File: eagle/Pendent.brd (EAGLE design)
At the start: 40.6 x 40.6 mm, 25 parts, among them Q1 CMA-4544PF-W, U1 Tiny85-20-SMT, U2 LF50ABDT-TR

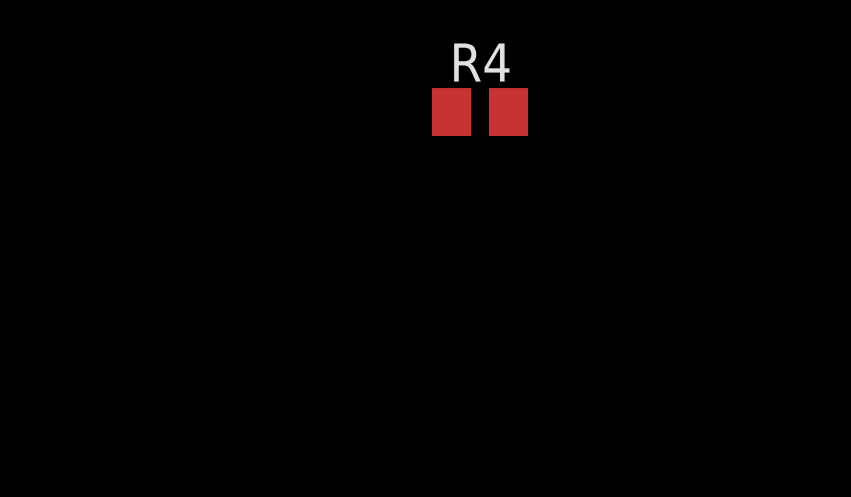
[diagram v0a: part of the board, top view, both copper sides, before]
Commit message: Add IRSend add IR LED to schematic
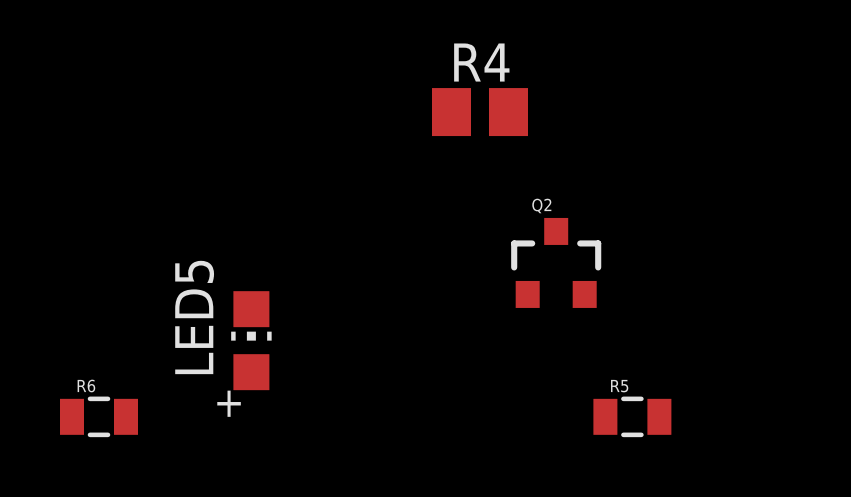
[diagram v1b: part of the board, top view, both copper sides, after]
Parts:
- added LED5: XZTNI54W, adafruit:CHIP-LED0805
- added Q2: MPSA42, SparkFun-DiscreteSemi:SOT23-3
- added R5: 1k, SparkFun-Passives:0805
- added R6: 20, SparkFun-Passives:0805
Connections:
- new net N$13: Q2.1, R5.2
- new net N$15: LED5.C, Q2.3
- new net N$16: LED5.A, R6.2
- new net N$17: R5.1, U1.6
- net GND: now also Q2.2
- net N$12: now also U1.7; no longer U1.6
- net N$4: now also U1.3; no longer U1.5
- net VCC: now also R6.1
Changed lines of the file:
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@@
 </element>
 <element name="R4" library="adafruit" package="M0805" value="" x="2.54" y="-40.64"/>
+<element name="Q2" library="SparkFun-DiscreteSemi" package="SOT23-3" value="MPSA42" x="5.08" y="-45.72">
+<attribute name="VALUE" value="MPSA42" x="5.08" y="-45.72" size="1.778" layer="27" display="off"/>
+<attribute name="PROD_ID" value="TRANS-09116" x="5.08" y="-45.72" size="1.778" layer="27" display="off"/>
+</element>
+<element name="R5" library="SparkFun-Passives" package="0805" value="1k" x="7.62" y="-50.8"/>
+<element name="LED5" library="adafruit" package="CHIP-LED0805" value="XZTNI54W" x="-5.08" y="-48.26"/>
+<element name="R6" library="SparkFun-Passives" package="0805" value="20" x="-10.16" y="-50.8"/>
 </elements>
 <signals>
@@
 <contactref element="S1" pad="3"/>
 <contactref element="S1" pad="4"/>
-<wire x1="31.545" y1="25" x2="31.545" y2="26.2" width="0" layer="19" extent="1-1"/>
-<wire x1="22.186" y1="22.86" x2="31.545" y2="25" width="0" layer="19" extent="1-1"/>
-<wire x1="20.283" y1="20.65" x2="22.186" y2="22.86" width="0" layer="19" extent="1-1"/>
-<wire x1="17.52" y1="16.28" x2="20.283" y2="20.65" width="0" layer="19" extent="1-1"/>
-<wire x1="15.864" y1="13.208" x2="17.52" y2="16.28" width="0" layer="19" extent="1-1"/>
-<wire x1="13.335" y1="10.4648" x2="15.864" y2="13.208" width="0" layer="19" extent="1-1"/>
+<contactref element="R6" pad="1"/>
+<wire x1="2.286" y1="-34.925" x2="-11.06" y2="-50.8" width="0" layer="19" extent="1-1"/>
+<wire x1="7.874" y1="-34.925" x2="2.286" y2="-34.925" width="0" layer="19" extent="1-1"/>
+<wire x1="9.16" y1="-27.94" x2="7.874" y2="-34.925" width="0" layer="19" extent="1-1"/>
+<wire x1="2.54" y1="7.962" x2="9.16" y2="-27.94" width="0" layer="19" extent="1-1"/>
+<wire x1="13.335" y1="10.4648" x2="2.54" y2="7.962" width="0" layer="19" extent="1-1"/>
+<wire x1="15.864" y1="13.208" x2="13.335" y2="10.4648" width="0" layer="19" extent="1-1"/>
+<wire x1="17.52" y1="16.28" x2="15.864" y2="13.208" width="0" layer="19" extent="1-1"/>
+<wire x1="20.283" y1="20.65" x2="17.52" y2="16.28" width="0" layer="19" extent="1-1"/>
+<wire x1="22.186" y1="22.86" x2="20.283" y2="20.65" width="0" layer="19" extent="1-1"/>
 <wire x1="22.186" y1="10.16" x2="15.864" y2="13.208" width="0" layer="19" extent="1-1"/>
-<wire x1="2.54" y1="7.962" x2="13.335" y2="10.4648" width="0" layer="19" extent="1-1"/>
+<wire x1="31.545" y1="25" x2="22.186" y2="22.86" width="0" layer="19" extent="1-1"/>
+<wire x1="31.545" y1="26.2" x2="31.545" y2="25" width="0" layer="19" extent="1-1"/>
 <wire x1="6.438" y1="23.368" x2="17.52" y2="16.28" width="0" layer="19" extent="1-1"/>
-<wire x1="9.16" y1="-27.94" x2="2.54" y2="7.962" width="0" layer="19" extent="1-1"/>
-<wire x1="7.874" y1="-34.925" x2="9.16" y2="-27.94" width="0" layer="19" extent="1-1"/>
-<wire x1="2.286" y1="-34.925" x2="7.874" y2="-34.925" width="0" layer="19" extent="1-1"/>
 </signal>
 <signal name="GND">
@@
 <contactref element="C11" pad="2"/>
 <contactref element="R4" pad="1"/>
+<contactref element="Q2" pad="2"/>
 <wire x1="34.495" y1="25.4" x2="34.32" y2="29.94" width="0" layer="19" extent="1-1"/>
 <wire x1="33.02" y1="25.4" x2="34.495" y2="25.4" width="0" layer="19" extent="1-1"/>
@@
 <wire x1="18.78" y1="-22.86" x2="11.16" y2="-27.94" width="0" layer="19" extent="1-1"/>
 <wire x1="1.59" y1="-40.64" x2="3.54" y2="-27.94" width="0" layer="19" extent="1-1"/>
+<wire x1="6.03" y1="-46.72" x2="1.59" y2="-40.64" width="0" layer="19" extent="1-1"/>
 </signal>
 <signal name="N$1">
@@
 </signal>
 <signal name="N$4">
-<contactref element="U1" pad="5"/>
 <contactref element="LED1" pad="4"/>
-<wire x1="17.145" y1="10.4648" x2="25.437" y2="20.65" width="0" layer="19" extent="1-1"/>
+<contactref element="U1" pad="3"/>
+<wire x1="15.875" y1="3.7338" x2="25.437" y2="20.65" width="0" layer="19" extent="1-1"/>
 </signal>
 <signal name="VDD">
@@
 <contactref element="S1" pad="1"/>
 <contactref element="S1" pad="2"/>
-<contactref element="U1" pad="6"/>
+<contactref element="U1" pad="7"/>
 <wire x1="2.286" y1="-31.115" x2="3.49" y2="-40.64" width="0" layer="19" extent="1-1"/>
 <wire x1="7.874" y1="-31.115" x2="2.286" y2="-31.115" width="0" layer="19" extent="1-1"/>
-<wire x1="15.875" y1="10.4648" x2="7.874" y2="-31.115" width="0" layer="19" extent="1-1"/>
+<wire x1="14.605" y1="10.4648" x2="7.874" y2="-31.115" width="0" layer="19" extent="1-1"/>
+</signal>
+<signal name="N$13">
+<contactref element="Q2" pad="1"/>
+<contactref element="R5" pad="2"/>
+<wire x1="8.52" y1="-50.8" x2="4.13" y2="-46.72" width="0" layer="19" extent="1-1"/>
+</signal>
+<signal name="N$15">
+<contactref element="Q2" pad="3"/>
+<contactref element="LED5" pad="C"/>
+<wire x1="5.08" y1="-44.62" x2="-5.08" y2="-47.21" width="0" layer="19" extent="1-1"/>
+</signal>
+<signal name="N$16">
+<contactref element="R6" pad="2"/>
+<contactref element="LED5" pad="A"/>
+<wire x1="-5.08" y1="-49.31" x2="-9.26" y2="-50.8" width="0" layer="19" extent="1-1"/>
+</signal>
+<signal name="N$17">
+<contactref element="U1" pad="6"/>
+<contactref element="R5" pad="1"/>
+<wire x1="15.875" y1="10.4648" x2="6.72" y2="-50.8" width="0" layer="19" extent="1-1"/>
 </signal>
 </signals>

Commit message: Board Layout
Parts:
- added JP10: (no value), SparkFun-Connectors:1X06
- added R7: 300, adafruit:M0805
- added S2: SWITCH-MOMENTARY-2SMD-REDUNDANT, SparkFun-Electromechanical:TACTILE-SWITCH-SMD
- C2, C3, C4, C5: device SparkFun-Capacitors:0603-CAP -> adafruit:C0805K
- C8, C9: device SparkFun-Capacitors:0805 -> adafruit:C0805K
- R4: value (none) -> 10k
- U$3: value (none) -> 6V; device adafruit:CR2032-SMD -> SparkFun-Electromechanical:BATTCON_20MM
- moved R6 79.3 mm to (36.6, 13.2), flipped to the bottom, turned to 270 degrees
- moved R5 69.1 mm to (33.5, 13.2), flipped to the bottom, turned to 270 degrees
- moved LED5 66.3 mm to (35.6, 4.06), flipped to the bottom, turned to 270 degrees
- moved Q2 62.1 mm to (35.1, 8.64), flipped to the bottom, turned to 180 degrees
- moved C10 51.8 mm to (23.9, 19.3), turned to 90 degrees
- moved R4 50.8 mm to (4.57, 10.2), flipped to the bottom
- moved C1 46.9 mm to (17.8, 23.4), turned to 90 degrees
- moved C6 45.1 mm to (13.7, 20.8), turned to 180 degrees
- moved C11 44.8 mm to (23.9, 14.7), turned to 270 degrees
- moved S1 38.6 mm to (6.60, 5.59), flipped to the bottom
- moved R3 36.0 mm to (13.7, 18.0)
- moved C7 35.7 mm to (20.8, 12.7), turned to 270 degrees
- moved R1 34.9 mm to (13.7, 15.2), turned to 180 degrees
- moved R2 31.3 mm to (17.3, 12.7), turned to 90 degrees
- moved Q1 27.0 mm to (7.87, 18.0), turned to 270 degrees
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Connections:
- removed net GAIN: U$1.P$10
- removed net N$12: R4.2, S1.1, S1.2, U1.7
- removed net N$17: R5.1, U1.6
- removed net VDD: LED2.1, LED3.1, LED4.1
- new net MISO: JP10.3, R5.1, U1.6
- new net MOSI: JP10.4, U1.5
- new net N$18: LED1.4, R7.1
- new net RST: JP10.1, S2.1, S2.2, U1.1
- new net SCK: JP10.2, R4.2, S1.1, S1.2, U1.7
- net GND: now also C2.2, C3.2, C4.2, C5.2, JP10.5, U$3.2; no longer C2.1, C3.1, C4.1, C5.1, U$3.-
- net N$2: now also LED2.2
- net N$3: now also LED3.2
- net N$4: now also R7.2; no longer LED1.4
- net N$6: now also U$3.1; no longer U$3.+$1, U$3.+$2
- net VCC: now also C2.1, C3.1, C4.1, C5.1, JP10.6, LED2.1, LED3.1, LED4.1, S2.3, S2.4, U$1.P$10; no longer C2.2, C3.2, C4.2, C5.2
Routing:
- net VCC: track 0.00 -> 175.7 mm, vias 0 -> 4
- net SCK: track 0.00 -> 60.6 mm, vias 0 -> 2
- net N$3: track 0.00 -> 45.4 mm
- net RST: track 0.00 -> 36.8 mm, vias 0 -> 2
- net N$6: track 0.00 -> 30.4 mm, vias 0 -> 1
- net MOSI: track 0.00 -> 29.0 mm
- net MISO: track 0.00 -> 27.7 mm, vias 0 -> 1
- net INPUT: track 0.00 -> 23.7 mm
- net N$4: track 0.00 -> 21.9 mm
- net N$22: track 0.00 -> 21.7 mm, vias 0 -> 2
- net N$2: track 0.00 -> 16.6 mm
- net N$16: track 0.00 -> 11.0 mm
- net N$14: track 0.00 -> 9.83 mm
- net GND: track 0.00 -> 7.35 mm, vias 0 -> 13
- net N$11: track 0.00 -> 6.81 mm
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- added copper zone on layer 1, net GND
- added copper zone on layer 16, net GND
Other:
- board text added: "GND"
- board text added: "RESET"
- board text added: "RST"
- board text added: "VCC"

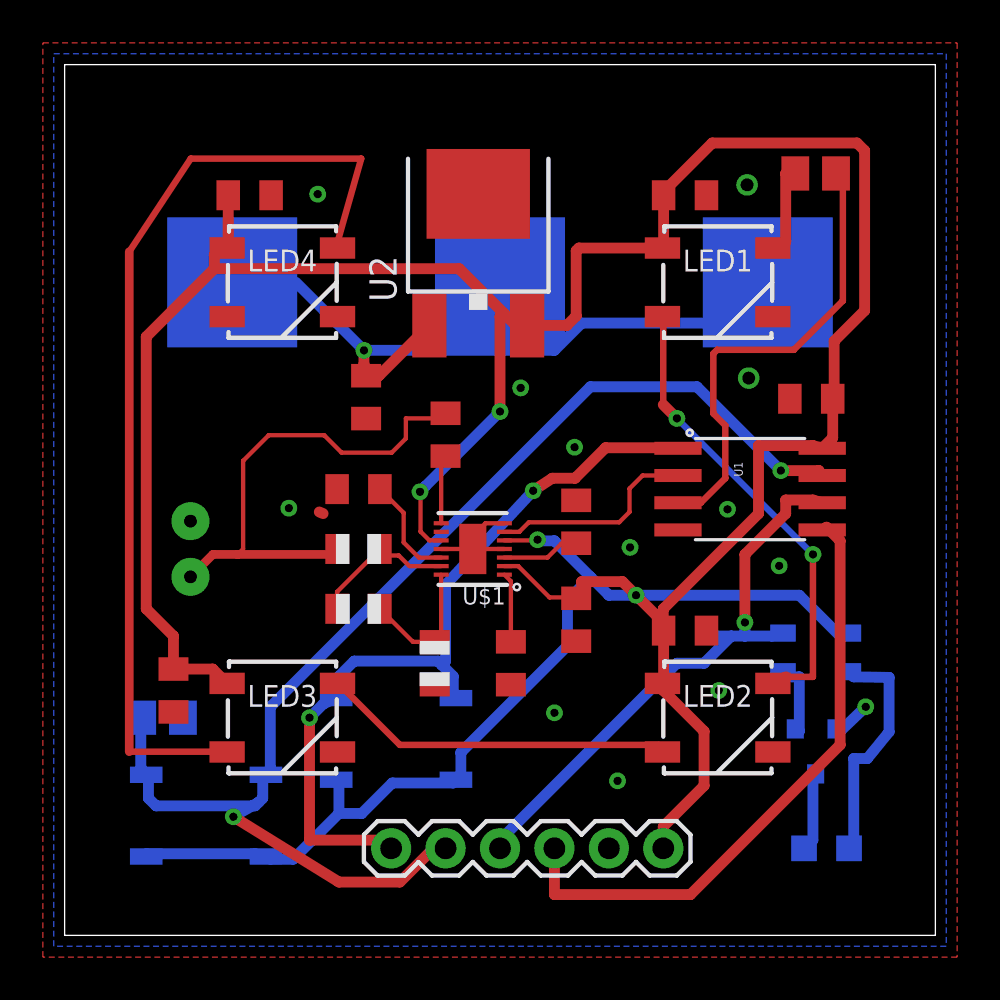
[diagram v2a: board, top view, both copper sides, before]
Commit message: Modificaitons to Board to Accomidate ATmega328P-AU
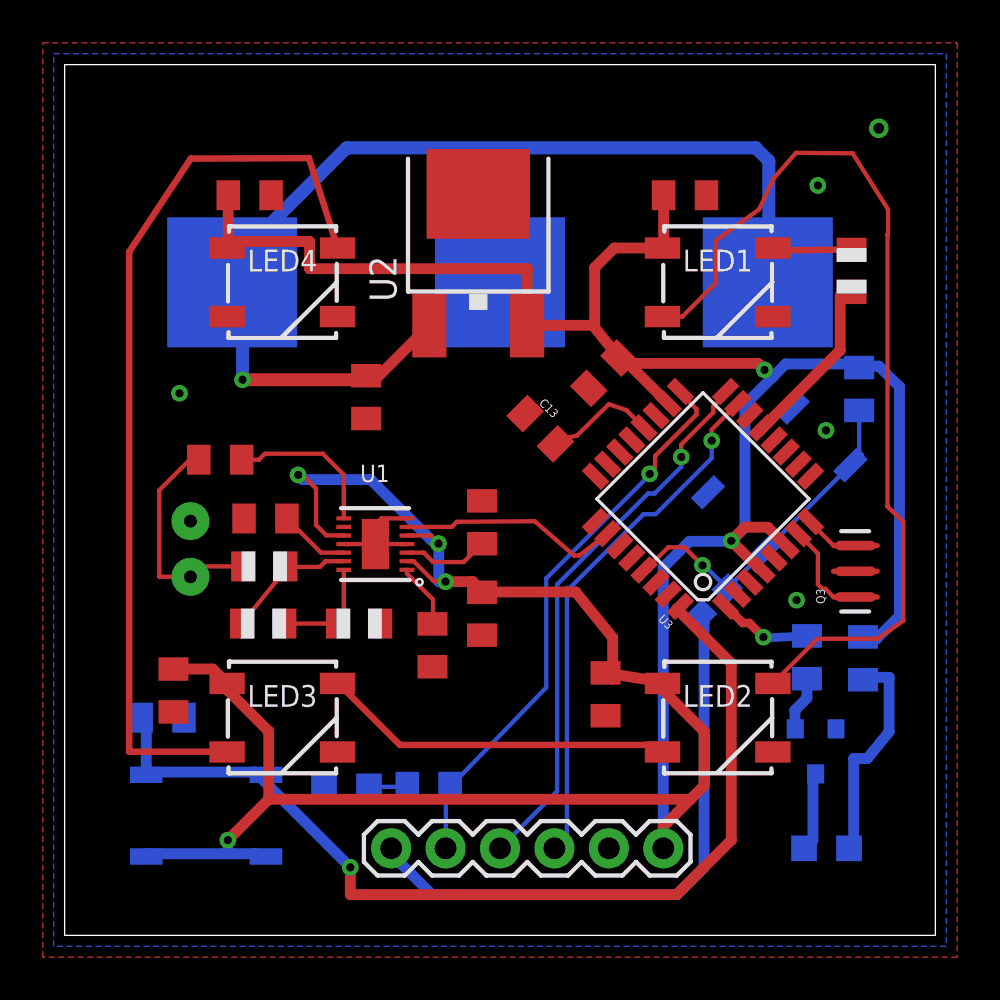
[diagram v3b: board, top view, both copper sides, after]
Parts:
- removed S2: SWITCH-MOMENTARY-2SMD-REDUNDANT, SparkFun-Electromechanical:TACTILE-SWITCH-SMD
- removed U$1: MAX9814TDFN14, adafruit:TDFN14_3X3MM
- added C13: 0.1uF, adafruit:C0805K
- added C14: 0.1uF, SparkFun:0603-CAP
- added D3: Green, adafruit:CHIPLED_0805
- added Q3: 8/16/20MHz, Testing:RESONATOR-SMD-1:1
- added R8: 10K, adafruit:R0805
- added R9: 330, adafruit:R0805
- added S3: RESET, Testing:TACTILE-SWITCH-SMD-ALT01
- added U3: ATMEGA328, SparkFun:TQFP32-08
- C8: value 0.1uF -> 2.2uF
- R4, R7: device adafruit:M0805 -> adafruit:R0805
- R5, R6: device SparkFun-Passives:0805 -> adafruit:R0805
- S1: value SWITCH-MOMENTARY-2SMD-REDUNDANT -> Tempo
- U1: value Tiny85-20-SMT -> MAX9814TDFN14; device SparkFun-DigitalIC:SO08-EIAJ -> adafruit:TDFN14_3X3MM
- moved U1 17.7 mm to (14.5, 18.3), turned to 180 degrees
- moved C1 10.6 mm to (7.26, 22.2), turned to 180 degrees
- moved C9 9.75 mm to (25.2, 26.2), turned to 225 degrees
- moved R7 4.85 mm to (36.7, 31.0), turned to 270 degrees
- moved C3 4.75 mm to (25.2, 11.3), turned to 270 degrees
- moved C6 4.55 mm to (9.37, 19.5)
- moved R1 4.50 mm to (9.27, 14.6)
- moved R3 4.47 mm to (9.32, 17.2)
- moved C11 4.40 mm to (19.5, 15.0)
- moved C10 4.39 mm to (19.5, 19.3)
- moved R2 3.99 mm to (13.7, 14.6), turned to 180 degrees
- moved C7 3.75 mm to (17.2, 13.5)
- moved R5 1.14 mm to (34.6, 13.0)
- moved R6 0.74 mm to (37.3, 12.9)
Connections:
- net N$6 renamed VBATT
- removed net N$14: U$1.P$6, U1.2
- removed net N$4: R7.2, U1.3
- new net A0: U3.23
- new net A1: U3.24
- new net A2: U3.25
- new net A3: U1.P$6, U3.26
- new net A6: U3.19
- new net A7: U3.22
- new net AREF: C13.2, U3.20
- new net D10: U3.14
- new net D2: R4.2, S1.1, S1.2, U3.32
- new net D3: R5.1, U3.1
- new net D4: U3.2
- new net D5: U3.9
- new net D6: U3.10
- new net D7: U3.11
- new net D8: U3.12
- new net D9: R7.2, U3.13
- new net N$1: D3.A, R9.2
- new net N$12: Q3.3, U3.8
- new net N$17: Q3.1, U3.7
- new net RESET: C14.1, R8.1, S3.3, S3.4, U3.29
- new net RXI: U3.30
- new net TXO: U3.31
- net A/R: now also U1.P$9; no longer U$1.P$9
- net GND: now also C13.1, D3.C, Q3.2, S3.1, S3.2, U1.P$11, U1.P$4, U1.P$7, U1.P$THERMAL, U3.21, U3.3, U3.5; no longer U$1.P$11, U$1.P$4, U$1.P$7, U$1.P$THERMAL, U1.4
- net MISO: now also U3.16; no longer R5.1, U1.6
- net MOSI: now also U3.15; no longer U1.5
- net N$10: now also U1.P$14; no longer U$1.P$14
- net N$11: now also U1.P$13; no longer U$1.P$13
- net N$5: now also U1.P$8; no longer U$1.P$8
- net N$7: now also U1.P$12; no longer U$1.P$12
- net N$8: now also U1.P$1; no longer U$1.P$1
- net N$9: now also U1.P$3; no longer U$1.P$3
- net RST: now also C14.2; no longer S2.1, S2.2, U1.1
- net SCK: now also R9.1, U3.17; no longer R4.2, S1.1, S1.2, U1.7
- net VCC: now also R8.2, U1.P$10, U1.P$2, U1.P$5, U3.18, U3.4, U3.6; no longer S2.3, S2.4, U$1.P$10, U$1.P$2, U$1.P$5, U1.8
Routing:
- net D2: track 0.00 -> 46.9 mm, vias 0 -> 1
- net SCK: track 60.6 -> 26.5 mm, vias 2 -> 1
- net N$4: track 21.9 -> 0.00 mm
- net N$22: track 21.7 -> 43.3 mm, vias 2 -> 0
- net VBATT: track 30.4 -> 48.2 mm
- net RESET: track 0.00 -> 16.0 mm, vias 0 -> 1
- net INPUT: track 23.7 -> 10.6 mm
- net A3: track 0.00 -> 10.4 mm
- net N$14: track 9.83 -> 0.00 mm
- net RST: track 36.8 -> 28.0 mm, vias 2 -> 0
- net D9: track 0.00 -> 8.74 mm
- net AREF: track 0.00 -> 5.37 mm
- net D3: track 0.00 -> 4.41 mm, vias 0 -> 1
- net MOSI: track 29.0 -> 24.8 mm, vias 0 -> 1
- net N$5: track 3.22 -> 7.32 mm
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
